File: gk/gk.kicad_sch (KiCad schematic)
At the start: 55 parts, among them J1 USB_C_Receptacle_USB2.0, J2 Conn_01x02, J8 Conn_ARM_JTAG_SWD_10, U1 WE-TVS-82400102, U2 MCP73831-2-OT, U3 AP62300WU

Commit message: Update pcb
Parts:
- added D5: D, Diode_SMD:D_SOD-128, symbol Device:D
- added D6: D_TVS, Diode_SMD:D_SMA, symbol Device:D_TVS
- added J10: Barrel_Jack_Switch, Connector_BarrelJack:BarrelJack_Horizontal, symbol Connector:Barrel_Jack_Switch
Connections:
- net GND: now also D6.1 (A1), J10.2, J10.3
- net at C3.1, D1.1 (K), D2.1 (K)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: now also D5.1 (K)
- new net: D5.2 (A), D6.2 (A2), J10.1
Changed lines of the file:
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@@
   (junction (at 93.98 33.02) (diameter 0) (color 0 0 0 0)
   )
+  (junction (at 146.05 45.72) (diameter 0) (color 0 0 0 0)
+  )
   (junction (at 116.84 45.72) (diameter 0) (color 0 0 0 0)
   )
@@
   (junction (at 63.5 53.34) (diameter 0) (color 0 0 0 0)
   )
+  (junction (at 124.46 80.01) (diameter 0) (color 0 0 0 0)
+  )
   (junction (at 257.81 72.39) (diameter 0) (color 0 0 0 0)
   )
@@
   (junction (at 217.17 40.64) (diameter 0) (color 0 0 0 0)
   )
+  (junction (at 124.46 87.63) (diameter 0) (color 0 0 0 0)
+  )
   (junction (at 138.43 139.7) (diameter 0) (color 0 0 0 0)
   )
@@
   (junction (at 59.69 153.67) (diameter 0) (color 0 0 0 0)
   )
+  (junction (at 116.84 85.09) (diameter 0) (color 0 0 0 0)
+  )
   (junction (at 58.42 33.02) (diameter 0) (color 0 0 0 0)
   )
@@
   )
   (junction (at 214.63 132.08) (diameter 0) (color 0 0 0 0)
+  )
+  (junction (at 158.75 72.39) (diameter 0) (color 0 0 0 0)
   )
   (junction (at 54.61 53.34) (diameter 0) (color 0 0 0 0)
@@
     (stroke (width 0) (type default))
   )
+  (wire (pts (xy 158.75 87.63) (xy 158.75 72.39))
+    (stroke (width 0) (type default))
+  )
   (wire (pts (xy 163.83 132.08) (xy 176.53 132.08))
     (stroke (width 0) (type default))
@@
     (stroke (width 0) (type default))
   )
+  (wire (pts (xy 119.38 85.09) (xy 119.38 87.63))
+    (stroke (width 0) (type default))
+  )
   (wire (pts (xy 60.96 72.39) (xy 81.28 72.39))
     (stroke (width 0) (type default))
@@
     (stroke (width 0) (type default))
   )
+  (wire (pts (xy 140.97 80.01) (xy 146.05 80.01))
+    (stroke (width 0) (type default))
+  )
   (wire (pts (xy 36.83 71.12) (xy 36.83 72.39))
     (stroke (width 0) (type default))
@@
     (stroke (width 0) (type default))
   )
-  (wire (pts (xy 168.91 72.39) (xy 147.32 72.39))
+  (wire (pts (xy 168.91 72.39) (xy 158.75 72.39))
     (stroke (width 0) (type default))
   )
@@
     (stroke (width 0) (type default))
   )
+  (wire (pts (xy 158.75 72.39) (xy 147.32 72.39))
+    (stroke (width 0) (type default))
+  )
   (wire (pts (xy 209.55 50.8) (xy 232.41 50.8))
     (stroke (width 0) (type default))
@@
     (stroke (width 0) (type default))
   )
+  (wire (pts (xy 116.84 80.01) (xy 124.46 80.01))
+    (stroke (width 0) (type default))
+  )
+  (wire (pts (xy 116.84 82.55) (xy 116.84 85.09))
+    (stroke (width 0) (type default))
+  )
   (wire (pts (xy 147.32 72.39) (xy 147.32 62.23))
     (stroke (width 0) (type default))
@@
     (stroke (width 0) (type default))
   )
+  (wire (pts (xy 124.46 87.63) (xy 158.75 87.63))
+    (stroke (width 0) (type default))
+  )
   (wire (pts (xy 62.23 139.7) (xy 74.93 139.7))
     (stroke (width 0) (type default))
@@
     (stroke (width 0) (type default))
   )
+  (wire (pts (xy 116.84 85.09) (xy 119.38 85.09))
+    (stroke (width 0) (type default))
+  )
   (wire (pts (xy 168.91 45.72) (xy 179.07 45.72))
     (stroke (width 0) (type default))
@@
     (stroke (width 0) (type default))
   )
+  (wire (pts (xy 124.46 80.01) (xy 133.35 80.01))
+    (stroke (width 0) (type default))
+  )
   (wire (pts (xy 147.32 39.37) (xy 160.02 39.37))
     (stroke (width 0) (type default))
@@
     (stroke (width 0) (type default))
   )
-  (wire (pts (xy 138.43 45.72) (xy 168.91 45.72))
+  (wire (pts (xy 138.43 45.72) (xy 146.05 45.72))
     (stroke (width 0) (type default))
   )
@@
     (stroke (width 0) (type default))
   )
+  (wire (pts (xy 119.38 87.63) (xy 124.46 87.63))
+    (stroke (width 0) (type default))
+  )
   (wire (pts (xy 240.03 139.7) (xy 252.73 139.7))
     (stroke (width 0) (type default))
@@
     (stroke (width 0) (type default))
   )
+  (wire (pts (xy 146.05 45.72) (xy 168.91 45.72))
+    (stroke (width 0) (type default))
+  )
   (wire (pts (xy 137.16 55.88) (xy 138.43 55.88))
     (stroke (width 0) (type default))
@@
   )
   (wire (pts (xy 257.81 40.64) (xy 267.97 40.64))
+    (stroke (width 0) (type default))
+  )
+  (wire (pts (xy 146.05 45.72) (xy 146.05 80.01))
     (stroke (width 0) (type default))
   )
@@
     )
   )
+  (symbol (lib_id "Device:D") (at 137.16 80.01 180) (unit 1)
+    (in_bom yes) (on_board yes) (dnp no) (fields_autoplaced)
+    (property "Reference" "D5" (at 137.16 74.93 0)
+      (effects (font (size 1.27 1.27)))
+    )
+    (property "Value" "D" (at 137.16 77.47 0)
+      (effects (font (size 1.27 1.27)))
+    )
+    (property "Footprint" "Diode_SMD:D_SOD-128" (at 137.16 80.01 0)
+      (effects (font (size 1.27 1.27)) hide)
+    )
+    (property "Datasheet" "~" (at 137.16 80.01 0)
+      (effects (font (size 1.27 1.27)) hide)
+    )
+    (property "Sim.Device" "D" (at 137.16 80.01 0)
+      (effects (font (size 1.27 1.27)) hide)
+    )
+    (property "Sim.Pins" "1=K 2=A" (at 137.16 80.01 0)
+      (effects (font (size 1.27 1.27)) hide)
+    )
+    (pin "1")
+    (pin "2")
+    (instances
+      (project "gk"
+        (path "/08730ac6-6084-459f-bdf1-86b322355ede"
+          (reference "D5") (unit 1)
+        )
+      )
+    )
+  )
   (symbol (lib_id "Device:C") (at 74.93 135.89 0) (unit 1)
     (in_bom yes) (on_board yes) (dnp no) (fields_autoplaced)
@@
         (path "/08730ac6-6084-459f-bdf1-86b322355ede"
           (reference "L1") (unit 1)
+        )
+      )
+    )
+  )
+  (symbol (lib_id "Device:D_TVS") (at 124.46 83.82 90) (unit 1)
+    (in_bom yes) (on_board yes) (dnp no) (fields_autoplaced)
+    (property "Reference" "D6" (at 127 82.5499 90)
+      (effects (font (size 1.27 1.27)) (justify right))
+    )
+    (property "Value" "D_TVS" (at 127 85.0899 90)
+      (effects (font (size 1.27 1.27)) (justify right))
+    )
+    (property "Footprint" "Diode_SMD:D_SMA" (at 124.46 83.82 0)
+      (effects (font (size 1.27 1.27)) hide)
+    )
+    (property "Datasheet" "~" (at 124.46 83.82 0)
+      (effects (font (size 1.27 1.27)) hide)
+    )
+    (pin "1")
+    (pin "2")
+    (instances
+      (project "gk"
+        (path "/08730ac6-6084-459f-bdf1-86b322355ede"
+          (reference "D6") (unit 1)
+        )
+      )
+      (project "MusicPlayer"
+        (path "/9538e4ed-27e6-4c37-b989-9859dc0d49e8"
+          (reference "D1") (unit 1)
         )
       )
@@
         )
       )
+    )
+  )
+  (symbol (lib_id "Connector:Barrel_Jack_Switch") (at 109.22 82.55 0) (unit 1)
+    (in_bom yes) (on_board yes) (dnp no) (fields_autoplaced)
+    (property "Reference" "J10" (at 109.22 74.93 0)
+      (effects (font (size 1.27 1.27)))
+    )
+    (property "Value" "Barrel_Jack_Switch" (at 109.22 77.47 0)
+      (effects (font (size 1.27 1.27)))
+    )
+    (property "Footprint" "Connector_BarrelJack:BarrelJack_Horizontal" (at 110.49 83.566 0)
+      (effects (font (size 1.27 1.27)) hide)
+    )
+    (property "Datasheet" "~" (at 110.49 83.566 0)
+      (effects (font (size 1.27 1.27)) hide)
+    )
+    (pin "1")
+    (pin "2")
+    (pin "3")
+    (instances
+      (project "gk"
+        (path "/08730ac6-6084-459f-bdf1-86b322355ede"
+          (reference "J10") (unit 1)
+        )
+      )

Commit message: Update pcb
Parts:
- added C79: 100n, Capacitor_SMD:C_0603_1608Metric, symbol Device:C
- added U10: MAX17048, Package_DFN_QFN:TDFN-8-1EP_2x2mm_P0.5mm_EP0.8x1.2mm, symbol gk-syms:MAX17048
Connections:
- net GND: now also C79.2, U10.1 (CTG), U10.4 (GND), U10.6 (QSTRT), U10.9 (GND2)
- net at C2.1, D1.2 (A), J2.1 (Pin_1)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: now also C79.1, U10.2 (CELL), U10.3 (VDD)
- new net I2C4_SCL: U10.7 (SCL)
- new net I2C4_SDA: U10.8 (SDA)
- no-connect marks 3 -> 4
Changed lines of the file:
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@@
   (junction (at 63.5 53.34) (diameter 0) (color 0 0 0 0)
   )
+  (junction (at 240.03 95.25) (diameter 0) (color 0 0 0 0)
+  )
   (junction (at 124.46 80.01) (diameter 0) (color 0 0 0 0)
   )
@@
   (junction (at 113.03 139.7) (diameter 0) (color 0 0 0 0)
   )
+  (junction (at 252.73 110.49) (diameter 0) (color 0 0 0 0)
+  )
   (junction (at 217.17 40.64) (diameter 0) (color 0 0 0 0)
   )
@@
   (junction (at 62.23 132.08) (diameter 0) (color 0 0 0 0)
   )
+  (junction (at 254 110.49) (diameter 0) (color 0 0 0 0)
+  )
   (junction (at 138.43 132.08) (diameter 0) (color 0 0 0 0)
   )
@@
   (junction (at 201.93 132.08) (diameter 0) (color 0 0 0 0)
   )
+  (junction (at 240.03 102.87) (diameter 0) (color 0 0 0 0)
+  )
   (junction (at 227.33 139.7) (diameter 0) (color 0 0 0 0)
   )
@@
   )
   (no_connect (at 52.07 60.96))
+  (no_connect (at 265.43 95.25))
   (no_connect (at 52.07 63.5))
   (no_connect (at 208.28 109.22))
@@
     (stroke (width 0) (type default))
   )
+  (wire (pts (xy 240.03 95.25) (xy 242.57 95.25))
+    (stroke (width 0) (type default))
+  )
   (wire (pts (xy 36.83 71.12) (xy 36.83 72.39))
     (stroke (width 0) (type default))
@@
     (stroke (width 0) (type default))
   )
+  (wire (pts (xy 229.87 95.25) (xy 240.03 95.25))
+    (stroke (width 0) (type default))
+  )
+  (wire (pts (xy 242.57 102.87) (xy 240.03 102.87))
+    (stroke (width 0) (type default))
+  )
+  (wire (pts (xy 252.73 109.22) (xy 252.73 110.49))
+    (stroke (width 0) (type default))
+  )
   (wire (pts (xy 55.88 29.21) (xy 63.5 29.21))
     (stroke (width 0) (type default))
@@
     (stroke (width 0) (type default))
   )
+  (wire (pts (xy 255.27 110.49) (xy 254 110.49))
+    (stroke (width 0) (type default))
+  )
   (wire (pts (xy 137.16 72.39) (xy 147.32 72.39))
     (stroke (width 0) (type default))
@@
     (stroke (width 0) (type default))
   )
+  (wire (pts (xy 240.03 102.87) (xy 240.03 110.49))
+    (stroke (width 0) (type default))
+  )
+  (wire (pts (xy 242.57 100.33) (xy 240.03 100.33))
+    (stroke (width 0) (type default))
+  )
   (wire (pts (xy 166.37 25.4) (xy 166.37 26.67))
     (stroke (width 0) (type default))
@@
     (stroke (width 0) (type default))
   )
+  (wire (pts (xy 240.03 110.49) (xy 252.73 110.49))
+    (stroke (width 0) (type default))
+  )
   (wire (pts (xy 29.21 72.39) (xy 36.83 72.39))
     (stroke (width 0) (type default))
@@
     (stroke (width 0) (type default))
   )
+  (wire (pts (xy 147.32 55.88) (xy 189.23 55.88))
+    (stroke (width 0) (type default))
+  )
   (wire (pts (xy 113.03 139.7) (xy 125.73 139.7))
     (stroke (width 0) (type default))
@@
     (stroke (width 0) (type default))
   )
+  (wire (pts (xy 189.23 55.88) (xy 189.23 80.01))
+    (stroke (width 0) (type default))
+  )
   (wire (pts (xy 54.61 48.26) (xy 54.61 45.72))
     (stroke (width 0) (type default))
@@
     (stroke (width 0) (type default))
   )
+  (wire (pts (xy 240.03 80.01) (xy 240.03 95.25))
+    (stroke (width 0) (type default))
+  )
   (wire (pts (xy 76.2 29.21) (xy 76.2 21.59))
     (stroke (width 0) (type default))
@@
     (stroke (width 0) (type default))
   )
+  (wire (pts (xy 189.23 80.01) (xy 240.03 80.01))
+    (stroke (width 0) (type default))
+  )
   (wire (pts (xy 138.43 45.72) (xy 146.05 45.72))
     (stroke (width 0) (type default))
@@
     (stroke (width 0) (type default))
   )
+  (wire (pts (xy 229.87 102.87) (xy 240.03 102.87))
+    (stroke (width 0) (type default))
+  )
   (wire (pts (xy 78.74 53.34) (xy 82.55 53.34))
     (stroke (width 0) (type default))
@@
     (stroke (width 0) (type default))
   )
+  (wire (pts (xy 252.73 110.49) (xy 254 110.49))
+    (stroke (width 0) (type default))
+  )
   (wire (pts (xy 232.41 50.8) (xy 232.41 49.53))
     (stroke (width 0) (type default))
@@
     (stroke (width 0) (type default))
   )
+  (wire (pts (xy 240.03 97.79) (xy 240.03 95.25))
+    (stroke (width 0) (type default))
+  )
   (wire (pts (xy 217.17 40.64) (xy 223.52 40.64))
     (stroke (width 0) (type default))
@@
     (stroke (width 0) (type default))
   )
+  (wire (pts (xy 242.57 97.79) (xy 240.03 97.79))
+    (stroke (width 0) (type default))
+  )
   (wire (pts (xy 81.28 50.8) (xy 81.28 72.39))
     (stroke (width 0) (type default))
@@
     (stroke (width 0) (type default))
   )
+  (wire (pts (xy 254 110.49) (xy 254 111.76))
+    (stroke (width 0) (type default))
+  )
+  (wire (pts (xy 255.27 109.22) (xy 255.27 110.49))
+    (stroke (width 0) (type default))
+  )
   (wire (pts (xy 147.32 55.88) (xy 147.32 39.37))
     (stroke (width 0) (type default))
@@
   )
   (wire (pts (xy 55.88 40.64) (xy 55.88 29.21))
+    (stroke (width 0) (type default))
+  )
+  (wire (pts (xy 240.03 100.33) (xy 240.03 102.87))
     (stroke (width 0) (type default))
   )
@@
     )
   )
+  (global_label "I2C4_SCL" (shape input) (at 265.43 100.33 0) (fields_autoplaced)
+    (effects (font (size 1.27 1.27)) (justify left))
+    (property "Intersheetrefs" "${INTERSHEET_REFS}" (at 277.1048 100.33 0)
+      (effects (font (size 1.27 1.27)) (justify left) hide)
+    )
+  )
   (global_label "USB_VBUS" (shape input) (at 102.87 33.02 0) (fields_autoplaced)
     (effects (font (size 1.27 1.27)) (justify left))
@@
     )
   )
+  (global_label "I2C4_SDA" (shape input) (at 265.43 97.79 0) (fields_autoplaced)
+    (effects (font (size 1.27 1.27)) (justify left))
+    (property "Intersheetrefs" "${INTERSHEET_REFS}" (at 277.1653 97.79 0)
+      (effects (font (size 1.27 1.27)) (justify left) hide)
+    )
+  )
   (global_label "SWCLK" (shape input) (at 208.28 101.6 0) (fields_autoplaced)
     (effects (font (size 1.27 1.27)) (justify left))
@@
         (path "/08730ac6-6084-459f-bdf1-86b322355ede"
           (reference "#FLG03") (unit 1)
+        )
+      )
+    )
+  )
+  (symbol (lib_id "power:GND") (at 254 111.76 0) (unit 1)
+    (in_bom yes) (on_board yes) (dnp no) (fields_autoplaced)
+    (property "Reference" "#PWR071" (at 254 118.11 0)
+      (effects (font (size 1.27 1.27)) hide)
+    )
+    (property "Value" "GND" (at 254 116.84 0)
+      (effects (font (size 1.27 1.27)))
+    )
+    (property "Footprint" "" (at 254 111.76 0)
+      (effects (font (size 1.27 1.27)) hide)
+    )
+    (property "Datasheet" "" (at 254 111.76 0)
+      (effects (font (size 1.27 1.27)) hide)
+    )
+    (pin "1")
+    (instances
+      (project "gk"
+        (path "/08730ac6-6084-459f-bdf1-86b322355ede"
+          (reference "#PWR071") (unit 1)
         )
       )
@@
     )
   )
+  (symbol (lib_id "Device:C") (at 229.87 99.06 0) (unit 1)
+    (in_bom yes) (on_board yes) (dnp no) (fields_autoplaced)
+    (property "Reference" "C79" (at 233.68 98.425 0)
+      (effects (font (size 1.27 1.27)) (justify left))
+    )
+    (property "Value" "100n" (at 233.68 100.965 0)
+      (effects (font (size 1.27 1.27)) (justify left))
+    )
+    (property "Footprint" "Capacitor_SMD:C_0603_1608Metric" (at 230.8352 102.87 0)
+      (effects (font (size 1.27 1.27)) hide)
+    )
+    (property "Datasheet" "~" (at 229.87 99.06 0)
+      (effects (font (size 1.27 1.27)) hide)
+    )
+    (pin "1")
+    (pin "2")
+    (instances
+      (project "gk"
+        (path "/08730ac6-6084-459f-bdf1-86b322355ede"
+          (reference "C79") (unit 1)
+        )
+      )
+    )
+  )
   (symbol (lib_id "power:GND") (at 176.53 35.56 0) (unit 1)
     (in_bom yes) (on_board yes) (dnp no) (fields_autoplaced)
@@
         )
       )
+    )
+  )
+  (symbol (lib_id "gk-syms:MAX17048") (at 254 90.17 0) (unit 1)
+    (in_bom yes) (on_board yes) (dnp no) (fields_autoplaced)
+    (property "Reference" "U10" (at 254 88.9 0)
+      (effects (font (size 1.27 1.27)))
+    )
+    (property "Value" "MAX17048" (at 254 91.44 0)
+      (effects (font (size 1.27 1.27)))
+    )
+    (property "Footprint" "Package_DFN_QFN:TDFN-8-1EP_2x2mm_P0.5mm_EP0.8x1.2mm" (at 254 91.44 0)
+      (effects (font (size 1.27 1.27)) hide)
+    )
+    (property "Datasheet" "" (at 254 90.17 0)
+      (effects (font (size 1.27 1.27)) hide)
+    )
+    (pin "1")
+    (pin "2")
+    (pin "3")
+    (pin "4")
+    (pin "5")
+    (pin "6")
+    (pin "7")
+    (pin "8")
+    (pin "9")
+    (instances
+      (project "gk"
+        (path "/08730ac6-6084-459f-bdf1-86b322355ede"
+          (reference "U10") (unit 1)
+        )
+      )

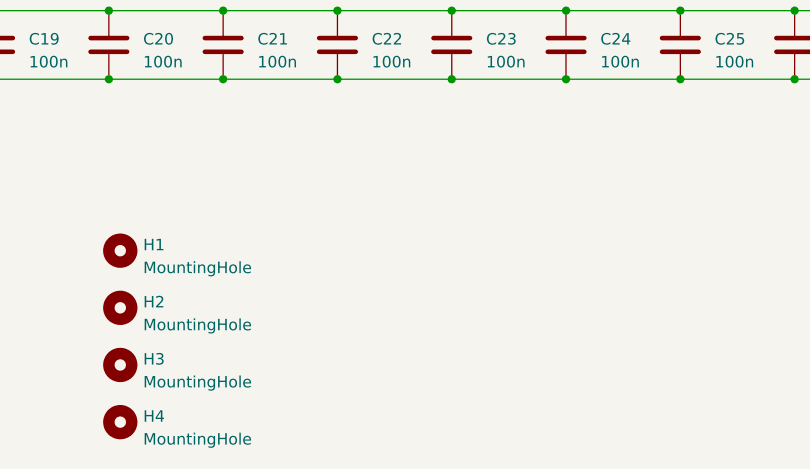
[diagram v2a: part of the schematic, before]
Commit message: Add mount pin for abxy/udlr buttons Fix button spacing Add leds for menu button
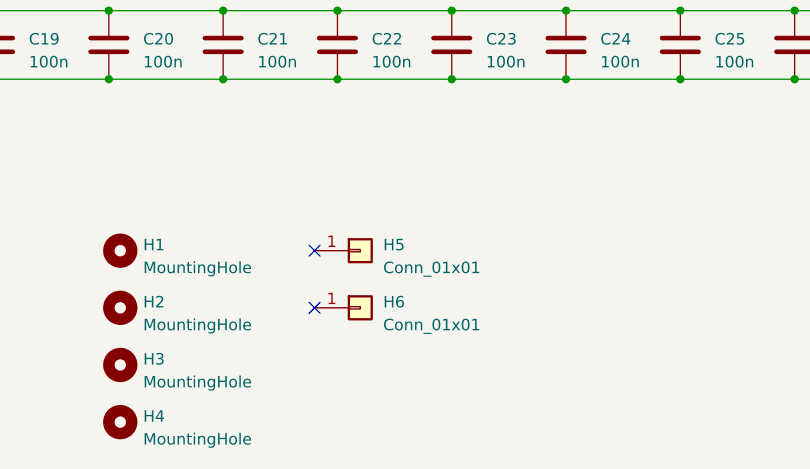
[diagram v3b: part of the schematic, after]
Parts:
- added H5, H6: Conn_01x01, Connector_PinHeader_2.54mm:PinHeader_1x01_P2.54mm_Vertical, symbol Connector_Generic:Conn_01x01
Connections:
- no-connect marks 4 -> 6
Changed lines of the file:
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@@
   (no_connect (at 265.43 95.25))
   (no_connect (at 52.07 63.5))
+  (no_connect (at 135.89 158.75))
   (no_connect (at 208.28 109.22))
+  (no_connect (at 135.89 165.1))
   (wire (pts (xy 147.32 55.88) (xy 147.32 59.69))
     (stroke (width 0) (type default))
@@
         (path "/08730ac6-6084-459f-bdf1-86b322355ede"
           (reference "#FLG03") (unit 1)
+        )
+      )
+    )
+  )
+  (symbol (lib_id "Connector_Generic:Conn_01x01") (at 140.97 158.75 0) (unit 1)
+    (in_bom yes) (on_board yes) (dnp no) (fields_autoplaced)
+    (property "Reference" "H5" (at 143.51 158.115 0)
+      (effects (font (size 1.27 1.27)) (justify left))
+    )
+    (property "Value" "Conn_01x01" (at 143.51 160.655 0)
+      (effects (font (size 1.27 1.27)) (justify left))
+    )
+    (property "Footprint" "Connector_PinHeader_2.54mm:PinHeader_1x01_P2.54mm_Vertical" (at 140.97 158.75 0)
+      (effects (font (size 1.27 1.27)) hide)
+    )
+    (property "Datasheet" "~" (at 140.97 158.75 0)
+      (effects (font (size 1.27 1.27)) hide)
+    )
+    (pin "1")
+    (instances
+      (project "gk"
+        (path "/08730ac6-6084-459f-bdf1-86b322355ede"
+          (reference "H5") (unit 1)
         )
       )
@@
         )
       )
+    )
+  )
+  (symbol (lib_id "Connector_Generic:Conn_01x01") (at 140.97 165.1 0) (unit 1)
+    (in_bom yes) (on_board yes) (dnp no) (fields_autoplaced)
+    (property "Reference" "H6" (at 143.51 164.465 0)
+      (effects (font (size 1.27 1.27)) (justify left))
+    )
+    (property "Value" "Conn_01x01" (at 143.51 167.005 0)
+      (effects (font (size 1.27 1.27)) (justify left))
+    )
+    (property "Footprint" "Connector_PinHeader_2.54mm:PinHeader_1x01_P2.54mm_Vertical" (at 140.97 165.1 0)
+      (effects (font (size 1.27 1.27)) hide)
+    )
+    (property "Datasheet" "~" (at 140.97 165.1 0)
+      (effects (font (size 1.27 1.27)) hide)
+    )
+    (pin "1")
+    (instances
+      (project "gk"
+        (path "/08730ac6-6084-459f-bdf1-86b322355ede"
+          (reference "H6") (unit 1)
+        )
+      )

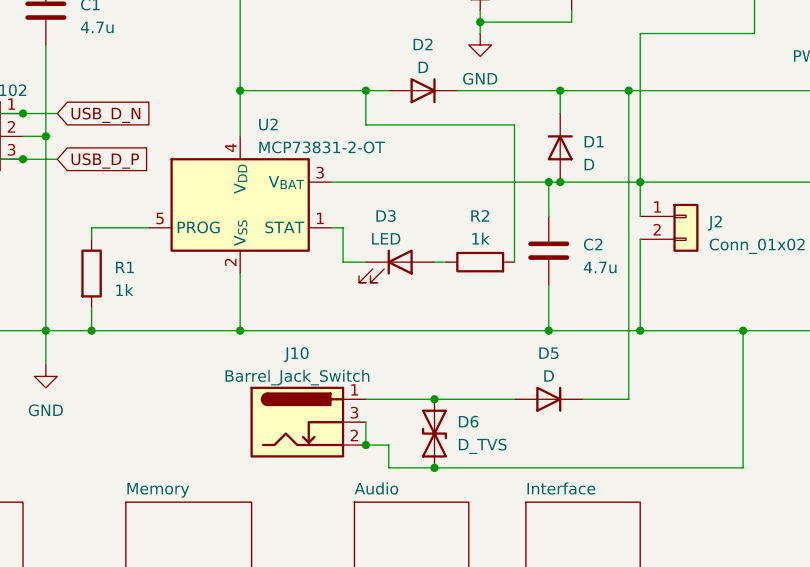
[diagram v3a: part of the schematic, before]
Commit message: Add vbat_stat detection
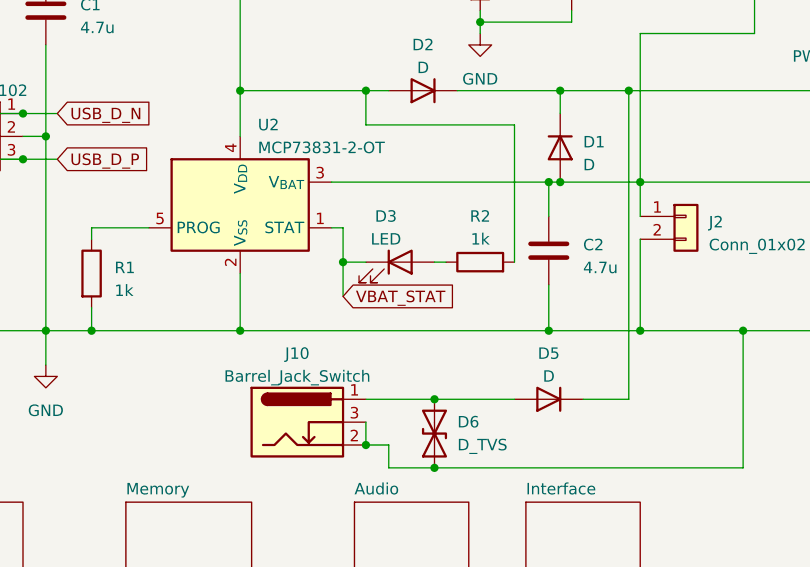
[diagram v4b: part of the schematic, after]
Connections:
- net VBAT_STAT: now reaches D3.1 (K), U2.1 (STAT)
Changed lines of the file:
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@@
   (junction (at 254 110.49) (diameter 0) (color 0 0 0 0)
+  )
+  (junction (at 114.3 64.77) (diameter 0) (color 0 0 0 0)
   )
   (junction (at 138.43 132.08) (diameter 0) (color 0 0 0 0)
@@
     (stroke (width 0) (type default))
   )
+  (wire (pts (xy 114.3 64.77) (xy 114.3 68.58))
+    (stroke (width 0) (type default))
+  )
   (wire (pts (xy 87.63 139.7) (xy 100.33 139.7))
     (stroke (width 0) (type default))
@@
       (effects (font (size 1.27 1.27)) (justify left) hide)
     )
+  )
+  (global_label "VBAT_STAT" (shape input) (at 114.3 68.58 0) (fields_autoplaced)
+    (effects (font (size 1.27 1.27)) (justify left))
+    (property "Intersheetrefs" "${INTERSHEET_REFS}" (at 126.8215 68.58 0)
+      (effects (font (size 1.27 1.27)) (justify left) hide)
+    )
